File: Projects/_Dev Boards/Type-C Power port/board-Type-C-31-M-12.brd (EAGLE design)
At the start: 18.5 x 23 mm, 2 parts, among them J1 USB-TYPE-C-31-M-12

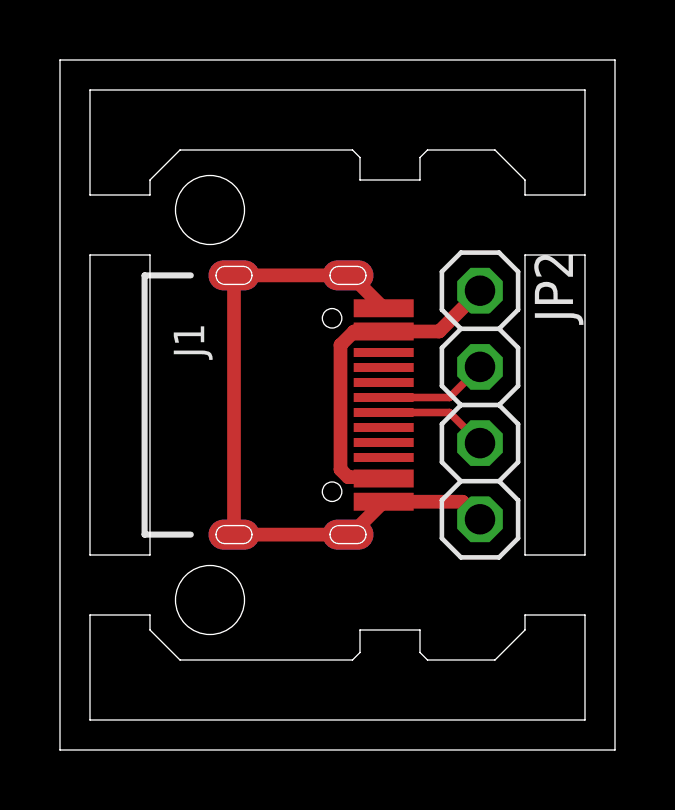
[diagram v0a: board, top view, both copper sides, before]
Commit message: updated Type-C power board
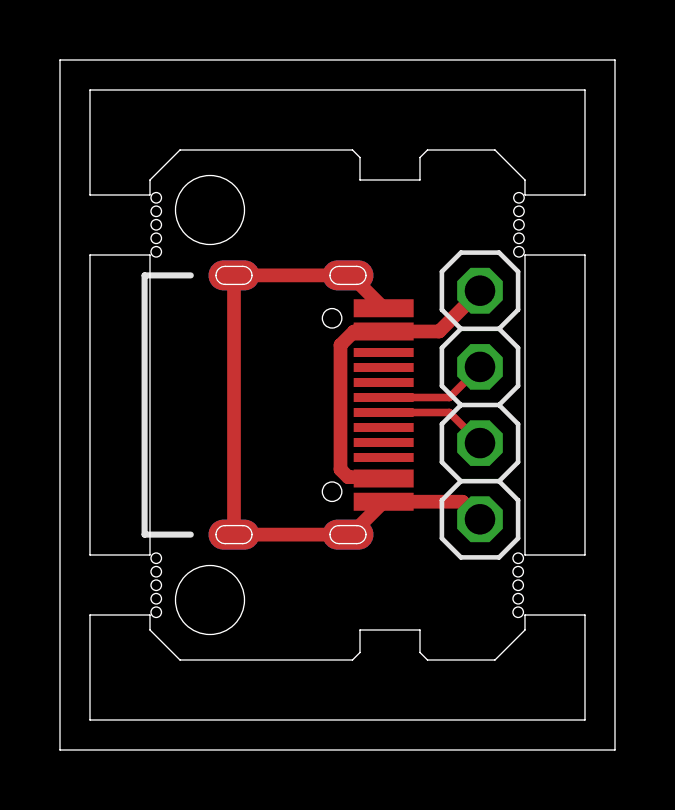
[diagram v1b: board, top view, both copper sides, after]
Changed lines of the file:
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@@
 <?xml version="1.0" encoding="utf-8"?>
 <!DOCTYPE eagle SYSTEM "eagle.dtd">
-<eagle version="9.6.0">
+<eagle version="9.6.1">
 <drawing>
 <settings>
@@
 <setting verticaltext="up"/>
 </settings>
-<grid distance="0.5" unitdist="mm" unit="mm" style="lines" multiple="1" display="yes" altdistance="5" altunitdist="mil" altunit="mil"/>
+<grid distance="1" unitdist="mil" unit="mil" style="lines" multiple="1" display="yes" altdistance="5" altunitdist="mil" altunit="mil"/>
 <layers>
 <layer number="1" name="Top" color="4" fill="1" visible="yes" active="yes"/>
@@
 <layer number="19" name="Unrouted" color="6" fill="1" visible="yes" active="yes"/>
 <layer number="20" name="Dimension" color="24" fill="1" visible="yes" active="yes"/>
-<layer number="21" name="tPlace" color="7" fill="1" visible="no" active="yes"/>
+<layer number="21" name="tPlace" color="7" fill="1" visible="yes" active="yes"/>
 <layer number="22" name="bPlace" color="7" fill="1" visible="yes" active="yes"/>
 <layer number="23" name="tOrigins" color="15" fill="1" visible="yes" active="yes"/>
 <layer number="24" name="bOrigins" color="15" fill="1" visible="yes" active="yes"/>
-<layer number="25" name="tNames" color="7" fill="1" visible="no" active="yes"/>
-<layer number="26" name="bNames" color="7" fill="1" visible="no" active="yes"/>
+<layer number="25" name="tNames" color="7" fill="1" visible="yes" active="yes"/>
+<layer number="26" name="bNames" color="7" fill="1" visible="yes" active="yes"/>
 <layer number="27" name="tValues" color="7" fill="1" visible="no" active="yes"/>
 <layer number="28" name="bValues" color="7" fill="1" visible="no" active="yes"/>
@@
 <wire x1="9.25" y1="17" x2="9" y2="16.75" width="0" layer="20"/>
 <wire x1="7" y1="16.75" x2="6.75" y2="17" width="0" layer="20"/>
-<dimension x1="0" y1="1" x2="12.5" y2="1" x3="6.25" y3="1" textsize="1.27" textratio="12" layer="21" width="0.08"/>
-<dimension x1="4.75" y1="0" x2="4.75" y2="17" x3="4.008" y3="8.5" textsize="1.27" textratio="12" layer="21" dtype="vertical" width="0.08"/>
-<dimension x1="0.85" y1="15" x2="3.15" y2="15" x3="2" y3="14.2" textsize="1.27" textratio="12" layer="21" width="0.08" extlength="0.5"/>
-<wire x1="0" y1="1" x2="7" y2="1" width="0.08" layer="22"/>
 <wire x1="9" y1="1" x2="12.5" y2="1" width="0.08" layer="22"/>
 <wire x1="7" y1="1.2" x2="9" y2="1.2" width="0.08" layer="22"/>
@@
 <wire x1="6.7" y1="17" x2="6.7" y2="16" width="0.08" layer="22"/>
 <text x="6.5" y="15.8" size="1.016" layer="22" font="vector" ratio="12" rot="MR0">1.0</text>
-<text x="12.06" y="13.63" size="1.27" layer="22" font="vector" ratio="15" rot="MR0">VBUS</text>
-<text x="9.41" y="10.16" size="1.27" layer="22" font="vector" ratio="12" rot="MR270" align="center">D+</text>
-<text x="9.45" y="6.66" size="1.27" layer="22" font="vector" ratio="12" rot="MR270" align="center">D-</text>
-<text x="12.06" y="2.51" size="1.27" layer="22" font="vector" ratio="15" rot="MR0">GND</text>
+<text x="8.9" y="13.56" size="1.27" layer="22" font="vector" ratio="15" rot="MR270" align="center">VBUS</text>
+<text x="8.9" y="9.66" size="1.27" layer="22" font="vector" ratio="12" rot="MR270" align="center">D+</text>
+<text x="8.9" y="7.16" size="1.27" layer="22" font="vector" ratio="12" rot="MR270" align="center">D-</text>
+<text x="8.9" y="4.06" size="1.27" layer="22" font="vector" ratio="15" rot="MR270" align="center">GND</text>
 <wire x1="-2" y1="-2" x2="-2" y2="1.5" width="0" layer="20"/>
 <wire x1="-2" y1="3.5" x2="-2" y2="13.5" width="0" layer="20"/>
@@
 <wire x1="15.5" y1="20" x2="-3" y2="20" width="0" layer="20"/>
 <wire x1="-3" y1="20" x2="-3" y2="-3" width="0" layer="20"/>
+<wire x1="0" y1="1" x2="7" y2="1" width="0.08" layer="22"/>
+<hole x="0.208" y="15.4066" drill="0.35"/>
+<hole x="0.208" y="14.9566" drill="0.35"/>
+<hole x="0.208" y="14.5066" drill="0.35"/>
+<hole x="0.208" y="14.0566" drill="0.35"/>
+<hole x="0.208" y="13.6066" drill="0.35"/>
+<hole x="12.2984" y="15.4066" drill="0.35"/>
+<hole x="12.2984" y="14.9566" drill="0.35"/>
+<hole x="12.2984" y="14.5066" drill="0.35"/>
+<hole x="12.2984" y="14.0566" drill="0.35"/>
+<hole x="12.2984" y="13.6066" drill="0.35"/>
+<hole x="12.273" y="3.3924" drill="0.35"/>
+<hole x="12.273" y="2.9424" drill="0.35"/>
+<hole x="12.273" y="2.4924" drill="0.35"/>
+<hole x="12.273" y="2.0424" drill="0.35"/>
+<hole x="12.273" y="1.5924" drill="0.35"/>
+<hole x="0.208" y="3.3924" drill="0.35"/>
+<hole x="0.208" y="2.9424" drill="0.35"/>
+<hole x="0.208" y="2.4924" drill="0.35"/>
+<hole x="0.208" y="2.0424" drill="0.35"/>
+<hole x="0.208" y="1.5924" drill="0.35"/>
 </plain>
 <attributes>
@@
 </class>
 </classes>
-<designrules name="default *">
+<designrules name="JLCPCB_2-Layer">
 <description language="de">&lt;b&gt;EAGLE Design Rules&lt;/b&gt;
 &lt;p&gt;
@@
 Einstellungen hier und speichern die Design Rules unter
 einem neuen Namen ab.</description>
-<description language="en">&lt;b&gt;EAGLE Design Rules&lt;/b&gt;
+<description language="en">&lt;b&gt;JLCPCB 2-layer PCB Design Rules&lt;/b&gt;
 &lt;p&gt;
-The default Design Rules have been set to cover
-a wide range of applications. Your particular design
-may have different requirements, so please make the
-necessary adjustments and save your customized
-design rules under a new name.</description>
+Source: &lt;a href=&quot;https://jlcpcb.com/capabilities/Capabilities&quot;&gt;JLCPCB specs&lt;/a&gt;
+&lt;/p&gt;</description>
 <param name="layerSetup" value="(1*16)"/>
 <param name="mtCopper" value="0.035mm 0.035mm 0.035mm 0.035mm 0.035mm 0.035mm 0.035mm 0.035mm 0.035mm 0.035mm 0.035mm 0.035mm 0.035mm 0.035mm 0.035mm 0.035mm"/>
 <param name="mtIsolate" value="1.5mm 0.15mm 0.2mm 0.15mm 0.2mm 0.15mm 0.2mm 0.15mm 0.2mm 0.15mm 0.2mm 0.15mm 0.2mm 0.15mm 0.2mm"/>
-<param name="mdWireWire" value="6mil"/>
-<param name="mdWirePad" value="6mil"/>
-<param name="mdWireVia" value="6mil"/>
-<param name="mdPadPad" value="6mil"/>
-<param name="mdPadVia" value="6mil"/>
-<param name="mdViaVia" value="6mil"/>
-<param name="mdSmdPad" value="6mil"/>
-<param name="mdSmdVia" value="6mil"/>
-<param name="mdSmdSmd" value="6mil"/>
+<param name="mdWireWire" value="5mil"/>
+<param name="mdWirePad" value="5mil"/>
+<param name="mdWireVia" value="5mil"/>
+<param name="mdPadPad" value="5mil"/>
+<param name="mdPadVia" value="5mil"/>
+<param name="mdViaVia" value="5mil"/>
+<param name="mdSmdPad" value="5mil"/>
+<param name="mdSmdVia" value="5mil"/>
+<param name="mdSmdSmd" value="5mil"/>
 <param name="mdViaViaSameLayer" value="6mil"/>
 <param name="mnLayersViaInSmd" value="2"/>
-<param name="mdCopperDimension" value="4mil"/>
-<param name="mdDrill" value="6mil"/>
+<param name="mdCopperDimension" value="8mil"/>
+<param name="mdDrill" value="3mil"/>
 <param name="mdSmdStop" value="0mil"/>
-<param name="msWidth" value="6mil"/>
-<param name="msDrill" value="0.35mm"/>
+<param name="msWidth" value="5mil"/>
+<param name="msDrill" value="0.2mm"/>
 <param name="msMicroVia" value="9.99mm"/>
 <param name="msBlindViaRatio" value="0.5"/>
@@
 <param name="rvMicroViaOuter" value="0.25"/>
 <param name="rvMicroViaInner" value="0.25"/>
-<param name="rlMinPadTop" value="10mil"/>
+<param name="rlMinPadTop" value="3mil"/>
 <param name="rlMaxPadTop" value="20mil"/>
-<param name="rlMinPadInner" value="10mil"/>
+<param name="rlMinPadInner" value="3mil"/>
 <param name="rlMaxPadInner" value="20mil"/>
-<param name="rlMinPadBottom" value="10mil"/>
+<param name="rlMinPadBottom" value="3mil"/>
 <param name="rlMaxPadBottom" value="20mil"/>
-<param name="rlMinViaOuter" value="8mil"/>
+<param name="rlMinViaOuter" value="0.2mm"/>
 <param name="rlMaxViaOuter" value="20mil"/>
-<param name="rlMinViaInner" value="8mil"/>
+<param name="rlMinViaInner" value="0.2mm"/>
 <param name="rlMaxViaInner" value="20mil"/>
 <param name="rlMinMicroViaOuter" value="4mil"/>
@@
 <param name="mlMinCreamFrame" value="0mil"/>
 <param name="mlMaxCreamFrame" value="0mil"/>
-<param name="mlViaStopLimit" value="0mil"/>
+<param name="mlViaStopLimit" value="15mil"/>
 <param name="srRoundness" value="0"/>
-<param name="srMinRoundness" value="0mil"/>
+<param name="srMinRoundness" value="1mil"/>
 <param name="srMaxRoundness" value="0mil"/>
-<param name="slThermalIsolate" value="10mil"/>
+<param name="slThermalIsolate" value="8mil"/>
 <param name="slThermalsForVias" value="0"/>
 <param name="dpMaxLengthDifference" value="10mm"/>
@@
 </autorouter>
 <elements>
-<element name="J1" library="angrypig7-Connectors" package="USB-TYPE-C-31-M-12" value="USB-TYPE-C-31-M-12" x="6.6" y="8.5" smashed="yes" rot="R270">
-<attribute name="NAME" x="0.79253125" y="11.23578125" size="1.016" layer="25" font="vector" ratio="12" rot="R270"/>
-</element>
+<element name="J1" library="angrypig7-Connectors" package="USB-TYPE-C-31-M-12" value="USB-TYPE-C-31-M-12" x="6.6" y="8.5" smashed="yes" rot="R270"/>
 <element name="JP2" library="pinhead_v2" package="1X04/OCT" value="" x="11" y="8.5" smashed="yes" rot="R270">
-<attribute name="NAME" x="12.8288" y="13.6562" size="1.27" layer="25" ratio="10" rot="R270"/>
 <attribute name="VALUE" x="7.825" y="13.58" size="1.27" layer="27" rot="R270"/>
 </element>

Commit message: update
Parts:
- removed JP2: (no value), pinhead_v2:1X04/OCT
- added JP1: (no value), angrypig7-Connectors-PinHeads:1X04
- added R1, R2: 5.1k, angrypig7-RCL:R0603
- moved J1 0.27 mm to (6.87, 8.50)
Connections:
- removed net N$1: J1.VBUS1, J1.VBUS2, JP2.1
- removed net N$4: J1.GND1, J1.GND2, J1.SHLD-B1, J1.SHLD-B2, J1.SHLD-B3, J1.SHLD-B4, J1.SHLD-T1, J1.SHLD-T2, J1.SHLD-T3, J1.SHLD-T4, JP2.4
- new net GND: J1.GND1, J1.GND2, J1.SHLD-B1, J1.SHLD-B2, J1.SHLD-B3, J1.SHLD-B4, J1.SHLD-T1, J1.SHLD-T2, J1.SHLD-T3, J1.SHLD-T4, JP1.4, R1.2, R2.2
- new net N$5: J1.A5, R1.1
- new net N$6: J1.B5, R2.1
- new net VBUS: J1.VBUS1, J1.VBUS2, JP1.1
- net N$2: now also J1.B6, JP1.2; no longer JP2.2
- net N$3: now also J1.B7, JP1.3; no longer JP2.3
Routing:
- net N$4: track 23.0 -> 0.00 mm
- net VBUS: track 0.00 -> 11.8 mm
- net N$1: track 11.1 -> 0.00 mm
- net N$6: track 0.00 -> 7.38 mm, vias 0 -> 1
- net N$5: track 0.00 -> 6.93 mm, vias 0 -> 1
- net N$3: track 3.63 -> 10.0 mm, vias 0 -> 1
- net GND: track 0.00 -> 3.21 mm, vias 0 -> 6
- net N$2: track 3.63 -> 6.73 mm
- added copper zone on layer 1, net GND
- added copper zone on layer 16, net GND

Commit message: update
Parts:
- J1: device angrypig7-Connectors:USB-TYPE-C-31-M-12 -> angrypig7-Connectors-USB:USB-TYPE-C-31-M-12
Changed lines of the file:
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@@
 <setting verticaltext="up"/>
 </settings>
-<grid distance="5" unitdist="mil" unit="mil" style="lines" multiple="1" display="yes" altdistance="5" altunitdist="mil" altunit="mil"/>
+<grid distance="10" unitdist="mil" unit="mil" style="lines" multiple="1" display="yes" altdistance="5" altunitdist="mil" altunit="mil"/>
 <layers>
 <layer number="1" name="Top" color="4" fill="1" visible="yes" active="yes"/>
@@
 </autorouter>
 <elements>
-<element name="J1" library="angrypig7-Connectors" package="USB-TYPE-C-31-M-12" package3d_urn="urn:adsk.eagle:package:24334474/2" value="USB-TYPE-C-31-M-12" x="6.866" y="8.5" smashed="yes" rot="R270"/>
+<element name="J1" library="angrypig7-Connectors-USB" package="USB-TYPE-C-31-M-12" package3d_urn="urn:adsk.eagle:package:24334474/2" value="USB-TYPE-C-31-M-12" x="6.866" y="8.5" smashed="yes" rot="R270"/>
 <element name="R1" library="angrypig7-RCL" package="R0603" package3d_urn="urn:adsk.eagle:package:23555/54" value="5.1k" x="3.962" y="9.389" smashed="yes" rot="MR0">
 <attribute name="NAME" x="3.962" y="10.659" size="1.27" layer="28" font="vector" ratio="15" rot="MR0" align="center"/>
